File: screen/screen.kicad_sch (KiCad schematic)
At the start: 40 parts

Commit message: update screen
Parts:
- removed C? (x2): 100nf, Capacitor_SMD:C_0402_1005Metric, symbol Device:C
- removed C? (x2): 10uf, Capacitor_SMD:C_0402_1005Metric, symbol Device:C
- removed D?: B120-E3, Diode_SMD:D_SOD-123, symbol Diode:B120-E3
- removed D?: RXD, LED_SMD:LED_0201_0603Metric, symbol Device:LED
- removed D?: TXD, LED_SMD:LED_0201_0603Metric, symbol Device:LED
- removed J?: J1, Connector_PinHeader_2.54mm:PinHeader_1x15_P2.54mm_Vertical, symbol Connector:Conn_01x15_Male
- removed J?: usbc, Connector_USB:USB_C_Receptacle_HRO_TYPE-C-31-M-12, symbol Connector:USB_C_Receptacle_USB2.0
- removed J?: J2, Connector_PinHeader_2.54mm:PinHeader_1x15_P2.54mm_Vertical, symbol Connector:Conn_01x15_Male
- removed Q?: q2, Package_TO_SOT_SMD:TSOT-23, symbol Device:Q_NPN_BEC
- removed Q?: q1, Package_TO_SOT_SMD:TSOT-23, symbol Device:Q_NPN_BEC
- removed R? (x3): 470, Resistor_SMD:R_0402_1005Metric, symbol Device:R
- removed R? (x2): 1k, Resistor_SMD:R_0402_1005Metric, symbol Device:R
- removed R? (x2): 12K, Resistor_SMD:R_0402_1005Metric, symbol Device:R
- removed SW?: SW_Push, myFootPrint:SMD,3x4x2mm, symbol Switch:SW_Push
- removed U?: CH340C, lc_lib:SOP-16_150MIL, symbol Interface_USB:CH340C
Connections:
- no-connect marks 20 -> 6
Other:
- note added: "KEY"
- note removed: "D0"
- note removed: "D1"
- note removed: "D10"
- note removed: "D2"
- note removed: "D3"
- note removed: "D4"
- note removed: "D5"
- note removed: "D6"
- note removed: "D7"
- note removed: "D8"
- note removed: "D9"
- note removed: "KEY-LED"
- note removed: "ONNECT"
- moved on the sheet: C?, R?, U?

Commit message: update
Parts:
- removed R?: 220K(1%), Resistor_SMD:R_0402_1005Metric, symbol Device:R
- removed R?: 100K(1%), Resistor_SMD:R_0402_1005Metric, symbol Device:R
- added J1: Conn_01x04_Female, Connector_PinHeader_1.00mm:PinHeader_1x04_P1.00mm_Vertical, symbol Connector:Conn_01x04_Female
- added J2: Conn_01x12_Female, Connector_PinHeader_1.00mm:PinHeader_1x04_P1.00mm_Vertical, symbol Connector:Conn_01x12_Female
- gave numbers to parts that had none: 17
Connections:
- net +3V3: now also J2.3 (Pin_3), J2.4 (Pin_4)
- net GND: now also J1.4 (Pin_4), J2.1 (Pin_1), J2.12 (Pin_12), J2.2 (Pin_2), J2.5 (Pin_5), J2.6 (Pin_6)
- net GPIO0: now also J1.3 (Pin_3), J2.7 (Pin_7)
- net GPIO13: now also J2.10 (Pin_10)
- net GPIO14: now also J2.9 (Pin_9)
- net nRST: now also J2.11 (Pin_11)
- new net RX: J1.1 (Pin_1)
- new net TX: J1.2 (Pin_2)
- no-connect marks 6 -> 7
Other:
- note added: "DC"
- note added: "SCL"
- note added: "SDA"

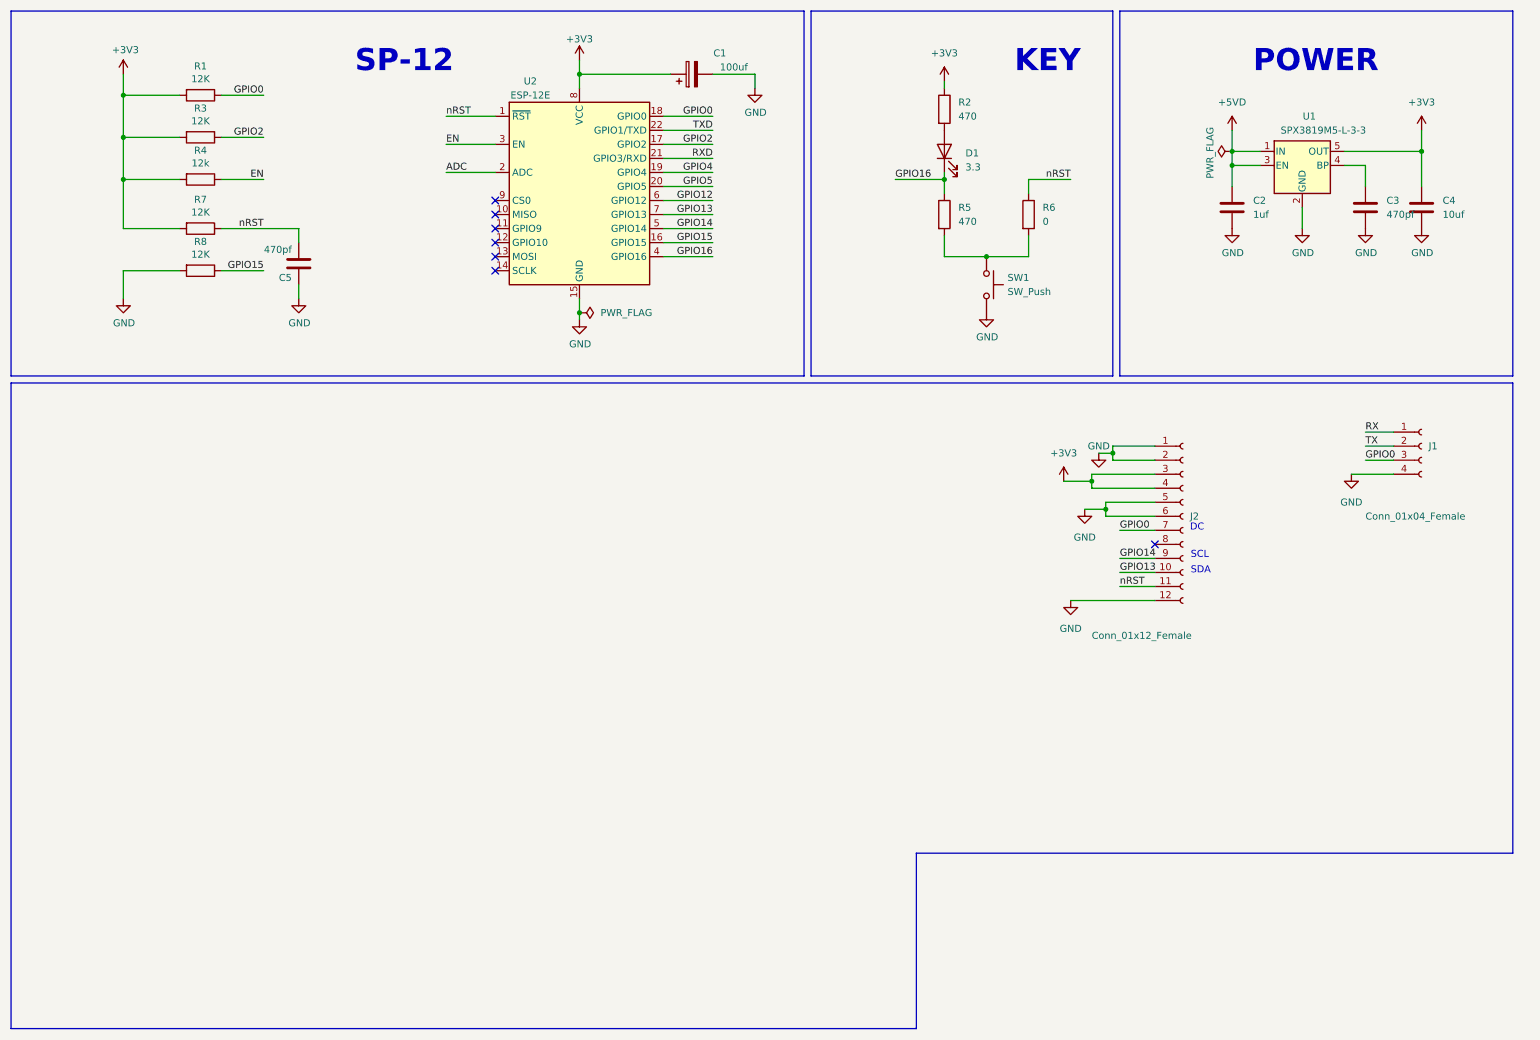
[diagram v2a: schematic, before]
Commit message: add tft footprint
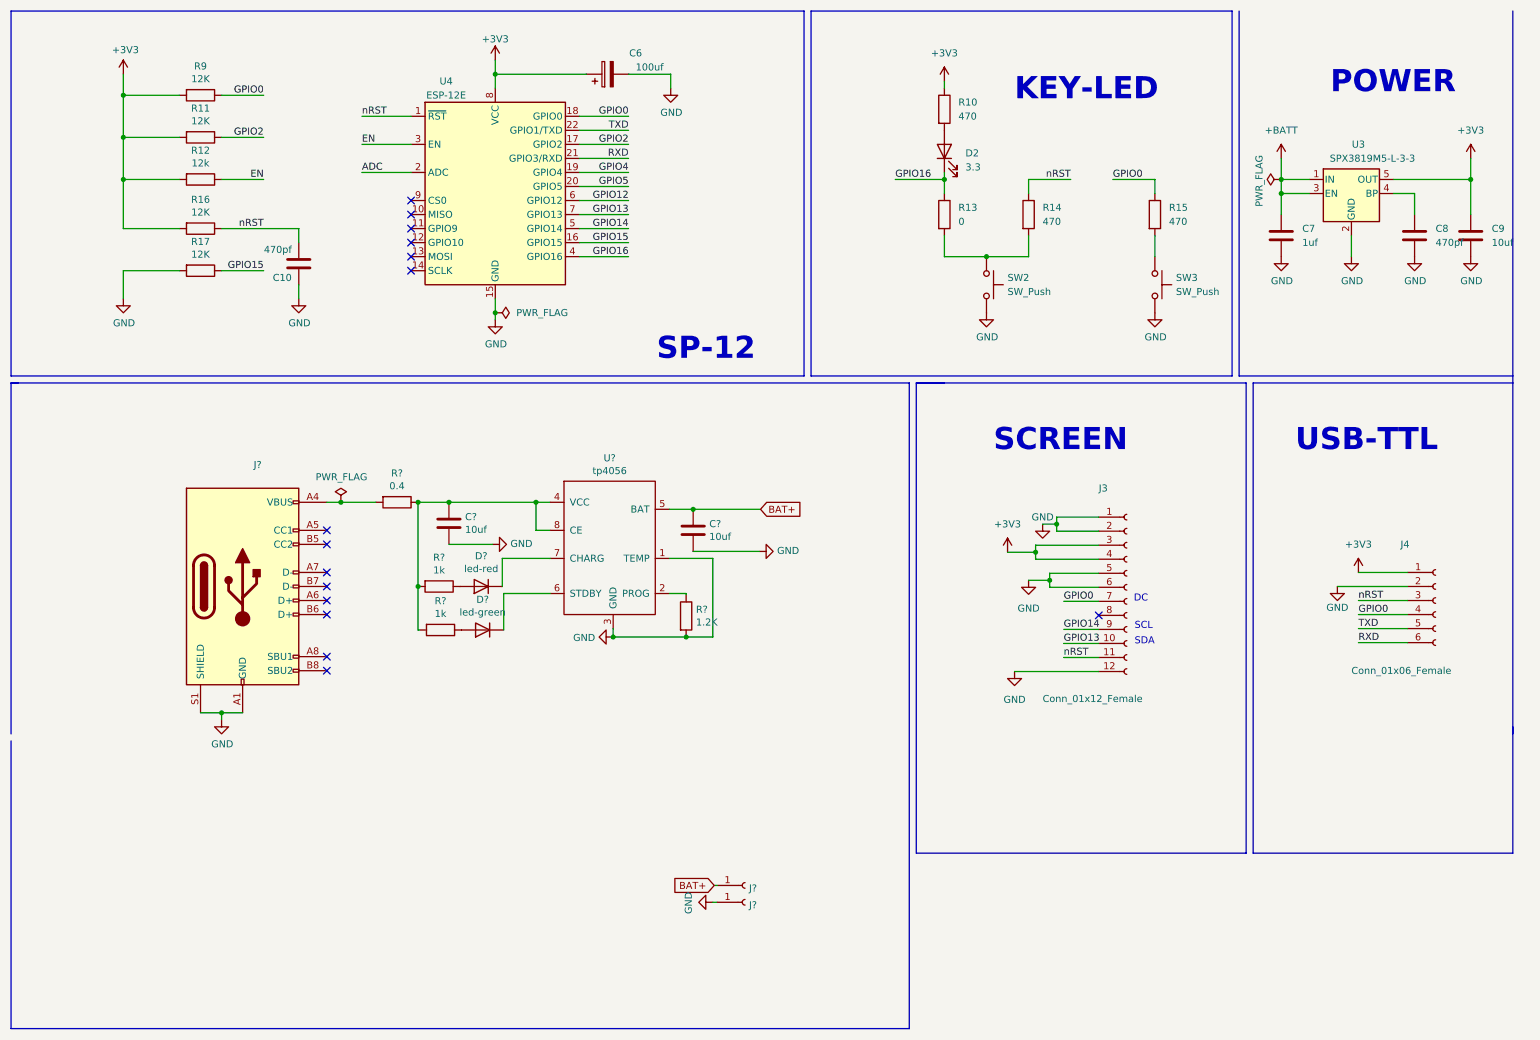
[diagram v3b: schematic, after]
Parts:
- removed C1: 100uf, lc_lib:CASE-B_3528, symbol Device:C_Polarized
- removed C2: 1uf, Capacitor_SMD:C_0402_1005Metric, symbol Device:C
- removed C3, C5: 470pf, Capacitor_SMD:C_0402_1005Metric, symbol Device:C
- removed C4: 10uf, Capacitor_SMD:C_0402_1005Metric, symbol Device:C
- removed D1: 3.3, LED_SMD:LED_0201_0603Metric, symbol Device:LED
- removed J1: Conn_01x04_Female, Connector_PinHeader_1.00mm:PinHeader_1x04_P1.00mm_Vertical, symbol Connector:Conn_01x04_Female
- removed J2: Conn_01x12_Female, Connector_PinHeader_1.00mm:PinHeader_1x04_P1.00mm_Vertical, symbol Connector:Conn_01x12_Female
- removed R1, R3, R7, R8: 12K, Resistor_SMD:R_0402_1005Metric, symbol Device:R
- removed R2, R5: 470, Resistor_SMD:R_0402_1005Metric, symbol Device:R
- removed R4: 12k, Resistor_SMD:R_0402_1005Metric, symbol Device:R
- removed R6: 0, Resistor_SMD:R_0402_1005Metric, symbol Device:R
- removed SW1: SW_Push, myFootPrint:SMD,3x4x2mm, symbol Switch:SW_Push
- removed U1: SPX3819M5-L-3-3, Package_TO_SOT_SMD:SOT-23-5, symbol Regulator_Linear:SPX3819M5-L-3-3
- removed U2: ESP-12E, RF_Module:ESP-12E, symbol RF_Module:ESP-12E
- added C10, C8: 470pf, Capacitor_SMD:C_0402_1005Metric, symbol Device:C
- added C6: 100uf, lc_lib:CASE-B_3528, symbol Device:C_Polarized
- added C7: 1uf, Capacitor_SMD:C_0402_1005Metric, symbol Device:C
- added C9: 10uf, Capacitor_SMD:C_0402_1005Metric, symbol Device:C
- added C? (x2): 10uf, Capacitor_SMD:C_0603_1608Metric, symbol Device:C
- added D2: 3.3, Capacitor_SMD:C_0402_1005Metric, symbol Device:LED
- added D?: led-red, LED_SMD:LED_0603_1608Metric, symbol Device:D
- added D?: led-green, LED_SMD:LED_0603_1608Metric, symbol Device:D
- added J3: Conn_01x12_Female, My-lib:TFT_1.4_12_back, symbol Connector:Conn_01x12_Female
- added J4: Conn_01x06_Female, Connector_PinHeader_2.54mm:PinHeader_1x06_P2.54mm_Vertical, symbol Connector:Conn_01x06_Female
- added J?: USB_C_Receptacle_USB2.0, Connector_USB:USB_C_Receptacle_HRO_TYPE-C-31-M-12, symbol Connector:USB_C_Receptacle_USB2.0
- added J? (x2): Conn_01x01_Female, my:largepoint, symbol Connector:Conn_01x01_Female
- added R10, R14, R15: 470, Resistor_SMD:R_0402_1005Metric, symbol Device:R
- added R11, R16, R17, R9: 12K, Resistor_SMD:R_0402_1005Metric, symbol Device:R
- added R12: 12k, Resistor_SMD:R_0402_1005Metric, symbol Device:R
- added R13: 0, Resistor_SMD:R_0402_1005Metric, symbol Device:R
- added R? (x2): 1k, Resistor_SMD:R_0603_1608Metric, symbol Device:R
- added R?: 0.4, Resistor_SMD:R_0603_1608Metric, symbol Device:R
- added R?: 1.2K, Resistor_SMD:R_0603_1608Metric, symbol Device:R
- added SW2, SW3: SW_Push, My-lib:SMD,3x4x2mm, symbol Switch:SW_Push
- added U3: SPX3819M5-L-3-3, Package_TO_SOT_SMD:SOT-23-5, symbol Regulator_Linear:SPX3819M5-L-3-3
- added U4: ESP-12E, RF_Module:ESP-12E, symbol RF_Module:ESP-12E
- added U?: tp4056, Package_SO:SOIC-8-1EP_3.9x4.9mm_P1.27mm_EP2.29x3mm, symbol my:tp4056
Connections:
- net +3V3: now also C6.1, C9.1, J3.3 (Pin_3), J3.4 (Pin_4), J4.1 (Pin_1), R10.1, R11.2, R12.2, R16.2, R9.2, U3.5 (OUT), U4.8 (VCC)
- net ADC: now also U4.2 (ADC)
- net EN: now also R12.1, U4.3 (EN)
- net GND: now also C10.1, C6.2, C7.2, C8.2, C9.2, C?.2, C?.2, J3.1 (Pin_1), J3.12 (Pin_12), J3.2 (Pin_2), J3.5 (Pin_5), J3.6 (Pin_6), J4.2 (Pin_2), J?.1 (Pin_1), J?.A1 (GND), J?.A12 (GND), J?.B1 (GND), J?.B12 (GND), J?.S1 (SHIELD), R17.2, R?.2, SW2.2, SW3.2, U3.2 (GND), U4.15 (GND), U?.1 (TEMP), U?.3 (GND)
- net GPIO0: now also J3.7 (Pin_7), J4.4 (Pin_4), R15.1, R9.1, U4.18 (GPIO0)
- net GPIO12: now also U4.6 (GPIO12)
- net GPIO13: now also J3.10 (Pin_10), U4.7 (GPIO13)
- net GPIO14: now also J3.9 (Pin_9), U4.5 (GPIO14)
- net GPIO15: now also R17.1, U4.16 (GPIO15)
- net GPIO16: now also D2.1 (K), R13.1, U4.4 (GPIO16)
- net GPIO2: now also R11.1, U4.17 (GPIO2)
- net GPIO4: now also U4.19 (GPIO4)
- net GPIO5: now also U4.20 (GPIO5)
- net RXD: now also J4.6 (Pin_6), U4.21 (GPIO3/RXD)
- net TXD: now also J4.5 (Pin_5), U4.22 (GPIO1/TXD)
- net nRST: now also C10.2, J3.11 (Pin_11), J4.3 (Pin_3), R14.1, R16.1, U4.1 (~{RST})
- new net: J?.A4 (VBUS), J?.A9 (VBUS), J?.B4 (VBUS), J?.B9 (VBUS), R?.2
- new net: D?.2 (A), R?.1 (x2)
- new net: C?.1, R?.1, R?.2, R?.2, U?.4 (VCC), U?.8 (CE)
- new net: R?.1, U?.2 (PROG)
- new net: R15.2, SW3.1
- new net: R13.2, R14.2, SW2.1
- new net: C8.1, U3.4 (BP)
- new net: D?.1 (K), U?.7 (CHARG)
- new net: D2.2 (A), R10.2
- new net: D?.1 (K), U?.6 (STDBY)
- new net +BATT: C7.1, U3.1 (IN), U3.3 (EN)
- new net BAT+: C?.1, J?.1 (Pin_1), U?.5 (BAT)
- no-connect marks 7 -> 15
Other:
- note added: "KEY-LED"
- note added: "SCREEN"
- note added: "USB-TTL"
- note removed: "KEY"
